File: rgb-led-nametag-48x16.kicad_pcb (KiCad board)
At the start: 4 copper layers, 84 x 28.8 mm, 160 parts, among them J1 USB_C_Receptacle_USB2.0, Q1 CJ3139K, Q10 CJ3139K, Q11 CJ3139K, Q12 CJ3139K, Q13 CJ3139K, Q14 CJ3139K, Q15 CJ3139K, Q16 CJ3139K, Q17 CJ3139K, Q18 CJ3139K, Q19 2SK3541, Q2 CJ3139K, Q20 AO3401A, Q3 CJ3139K, Q4 CJ3139K, Q5 CJ3139K, Q6 CJ3139K, Q7 CJ3139K, Q8 CJ3139K, Q9 CJ3139K, SW1 SW_Push, SW2 SW_Push, U1 led-panel-16x16, U10 74HC595, U11 74HC595, U12 74HC595, U13 74HC595, U14 74HC595, U15 74HC595, U16 led-panel-16x16, U17 74HC595, U18 74HC595, U19 74HC595, U2 74HC595, U20 74HC595, U21 74HC595, U22 74HC595, U23 74HC595, U24 ESP32-PICO-D4, U25 STM32F722RETx, U26 SRV05-4, U27 TPS63001, U28 XC6206P332MR, U3 74HC595, U4 74HC595, U5 74HC595, U6 74HC595, U7 74HC595, U8 74HC595, U9 led-panel-16x16

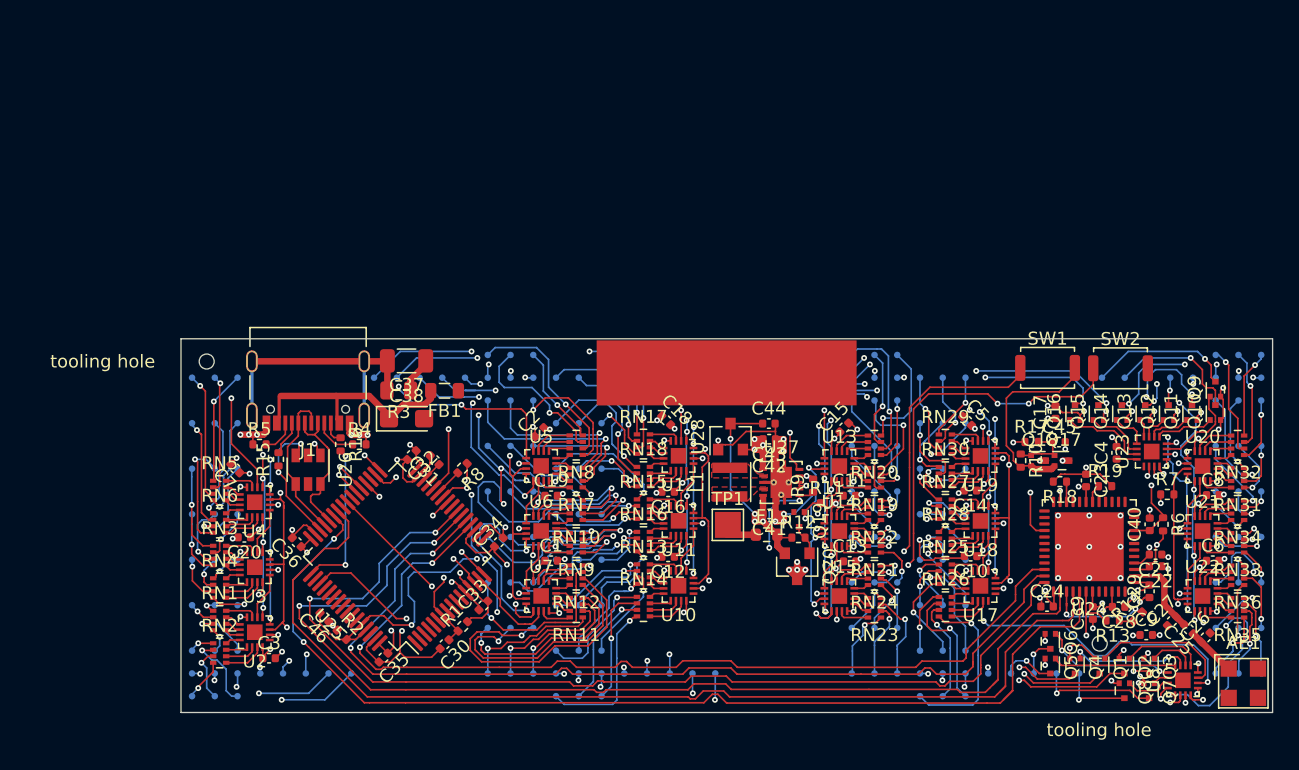
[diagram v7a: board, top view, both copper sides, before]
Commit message: Add primary battery protection
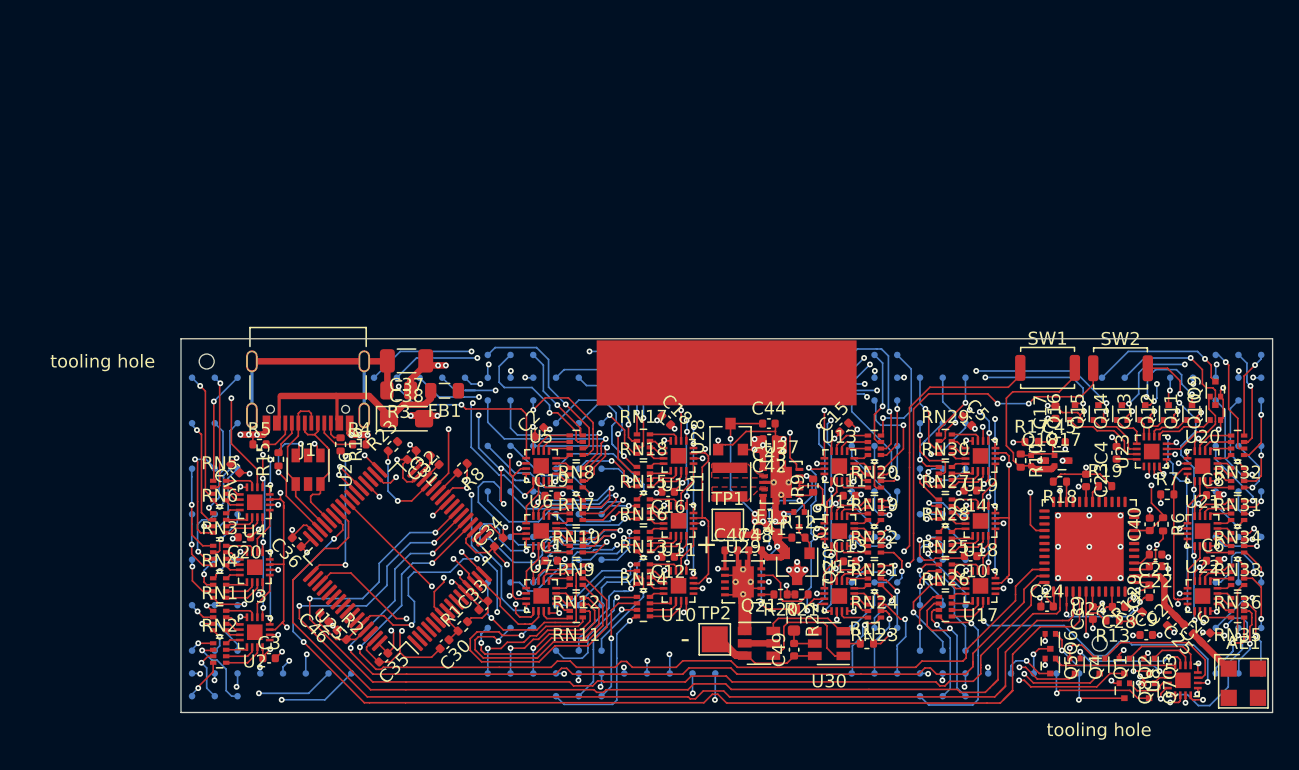
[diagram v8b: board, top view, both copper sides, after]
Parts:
- added C47: 1uF, Capacitor_SMD:C_0402_1005Metric, F.Cu at (133.8, 111.0)
- added C48: 100nF, Capacitor_SMD:C_0402_1005Metric, F.Cu at (135.6, 111.0)
- added C49: 100nF, Capacitor_SMD:C_0402_1005Metric, F.Cu at (138.6, 118.6)
- added Q21: FS8205, Package_TO_SOT_SMD:SOT-23-6, F.Cu at (135.9, 118.2)
- added R20: 1.5k, Resistor_SMD:R_0402_1005Metric, F.Cu at (137.6, 114.4)
- added R21: 10k, Resistor_SMD:R_0402_1005Metric, F.Cu at (139.2, 114.4)
- added R22: 470R, Resistor_SMD:R_0603_1608Metric, F.Cu at (138.6, 116.3)
- added R23: 10k, Resistor_SMD:R_0402_1005Metric, F.Cu at (107.7, 103.0)
- added TP2: BAT-, TestPoint:TestPoint_Pad_2.0x2.0mm, F.Cu at (132.5, 117.8)
- added U29: BQ24081, Package_SON:Texas_DRC0010J_ThermalVias, F.Cu at (134.7, 113.4)
- added U30: DW01+G, Package_TO_SOT_SMD:SOT-23-6, F.Cu at (141.3, 118.2)
- R11: value 100k -> 1k
- RN1, RN10, RN11, RN12, RN13, RN14, RN15, RN16, RN17, RN18, RN19, RN2, RN20, RN21, RN22, RN23, RN24, RN25, RN26, RN27, RN28, RN29, RN3, RN30, RN31, RN32, RN33, RN34, RN35, RN36, RN4, RN5, RN6, RN7, RN8, RN9: value 56R -> 220R
- moved R11 11.2 mm to (144.2, 118.2)
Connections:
- net /VBAT+ renamed +BATT
- C46 pad 1: GND -> /DFU
- C46 pad 2: /DFU -> GND
- Q19 pad 1: /VBUS_EN -> /PWR_EN
- R11 pad 1: /VBUS_EN -> Net-(R11-Pad1)
- U25 pad 29: /ROW_~OE -> /USB_SENSE
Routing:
- net GND: track 109.9 -> 135.2 mm, vias 63 -> 73
- net +BATT: track 28.5 -> 41.6 mm, vias 6 -> 7
- net Net-(C49-Pad1): track 0.00 -> 12.3 mm
- net Net-(Q21-Pad4): track 0.00 -> 9.47 mm
- net /USB_SENSE: track 0.00 -> 7.10 mm, vias 0 -> 2
- net +5V: track 0.00 -> 7.00 mm, vias 0 -> 2
- net Net-(Q21-Pad6): track 0.00 -> 6.73 mm
- net Net-(R21-Pad1): track 0.00 -> 5.35 mm
- net Net-(C49-Pad2): track 0.00 -> 2.65 mm
- net /COL_~OE: track 201.7 -> 199.1 mm
- net Net-(Q21-Pad2): track 0.00 -> 2.20 mm
- net /VBUS_EN: track 2.05 -> 0.00 mm, vias 1 -> 0
- net /QSPI_CLK: track 173.2 -> 175.0 mm
- net Net-(R11-Pad1): track 0.00 -> 1.41 mm
- net /PWR_EN: track 39.2 -> 40.2 mm
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- added copper zone on In1.Cu, net GND
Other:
- board text added: "+"
- board text added: "-"
